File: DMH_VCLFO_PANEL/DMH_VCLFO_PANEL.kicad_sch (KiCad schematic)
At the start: 44 parts, among them J0 Panel_GND_Solder_Wire_Pad

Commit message: Improved ergonomics
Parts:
- removed H17, H27, H6: Square, SynthStuff:Jack_6.35mm_Cutout_Output_v6, symbol SynthStuff:MountingHole_Jack6.35mm_Output_v2
- removed H19, H29, H7: Triangle, SynthStuff:Jack_6.35mm_Cutout_Output_v6, symbol SynthStuff:MountingHole_Jack6.35mm_Output_v2
- added H17, H27, H7: Rmp/Rnd, SynthStuff:Toggle_Switch_TE_Cutout, symbol SynthStuff:MountingHole_ToggleSwitch
- added H19, H29, H6: Sin/Tri, SynthStuff:Toggle_Switch_TE_Cutout, symbol SynthStuff:MountingHole_ToggleSwitch
- H10, H23, H33: value Sine -> Ramp / Random
- H11, H24, H34: value Random -> Triangle / Sine
- H22, H32, H9: value Ramp -> Saw
- H39, H40, H8: value Saw -> Square
- H44, H45, H46: value Unipolar -> Pol
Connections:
- net GND: now also H17.1, H19.1, H27.1, H29.1, H6.1, H7.1

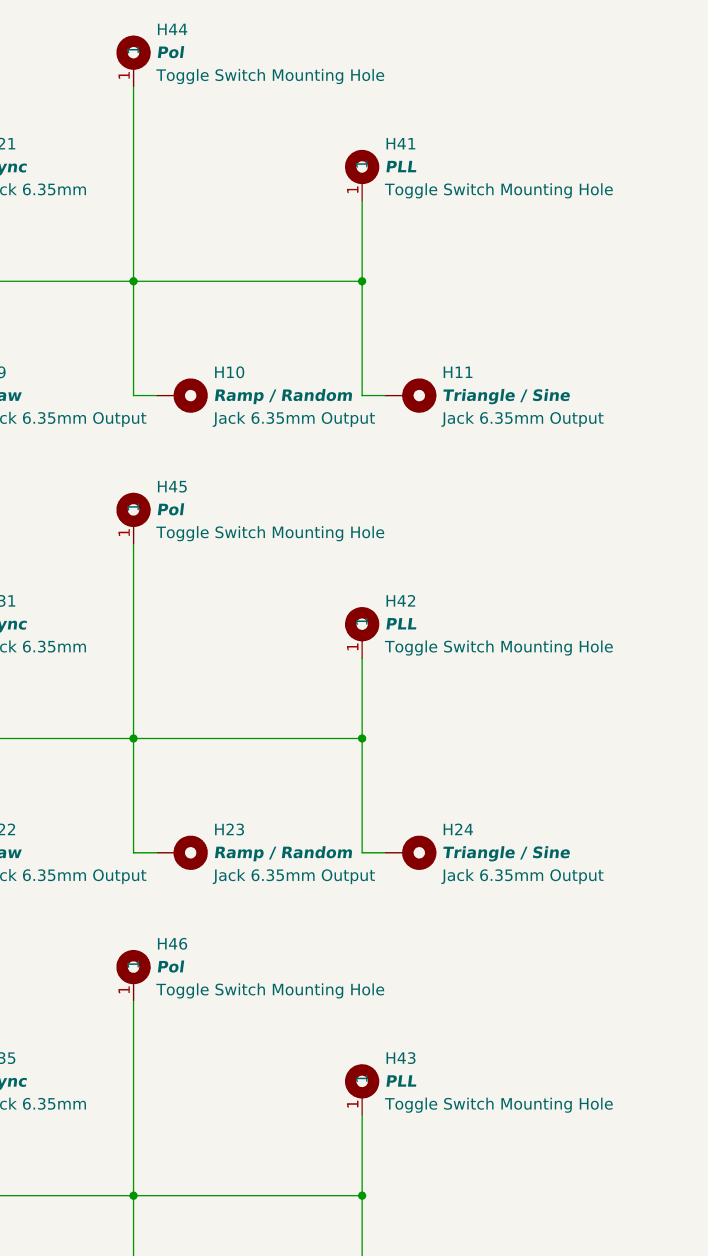
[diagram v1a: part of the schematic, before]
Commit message: Replaced PLL with Range
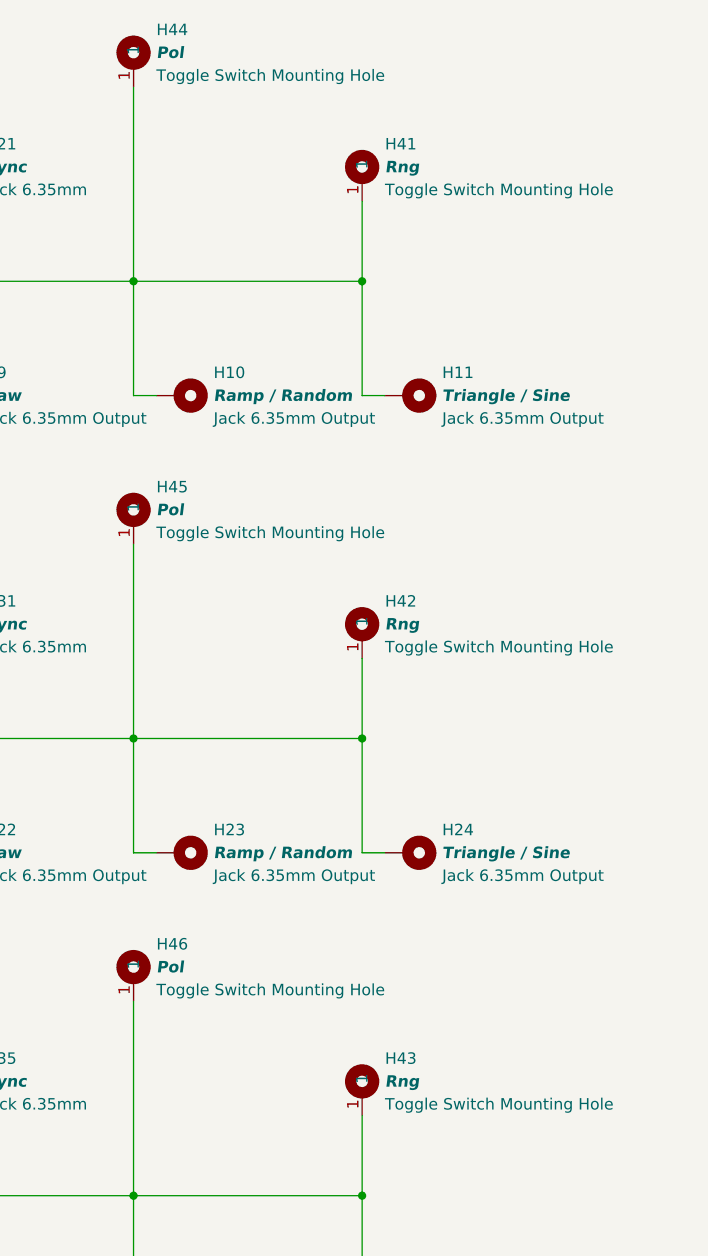
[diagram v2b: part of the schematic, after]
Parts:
- H41, H42, H43: value PLL -> Rng
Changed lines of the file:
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@@
 			)
 		)
-		(property "Value" "PLL"
+		(property "Value" "Rng"
 			(at 161.29 50.8 0)
 			(effects
@@
 			)
 		)
-		(property "Value" "PLL"
+		(property "Value" "Rng"
 			(at 161.29 101.6 0)
 			(effects
@@
 			)
 		)
-		(property "Value" "PLL"
+		(property "Value" "Rng"
 			(at 161.29 152.4 0)
 			(effects

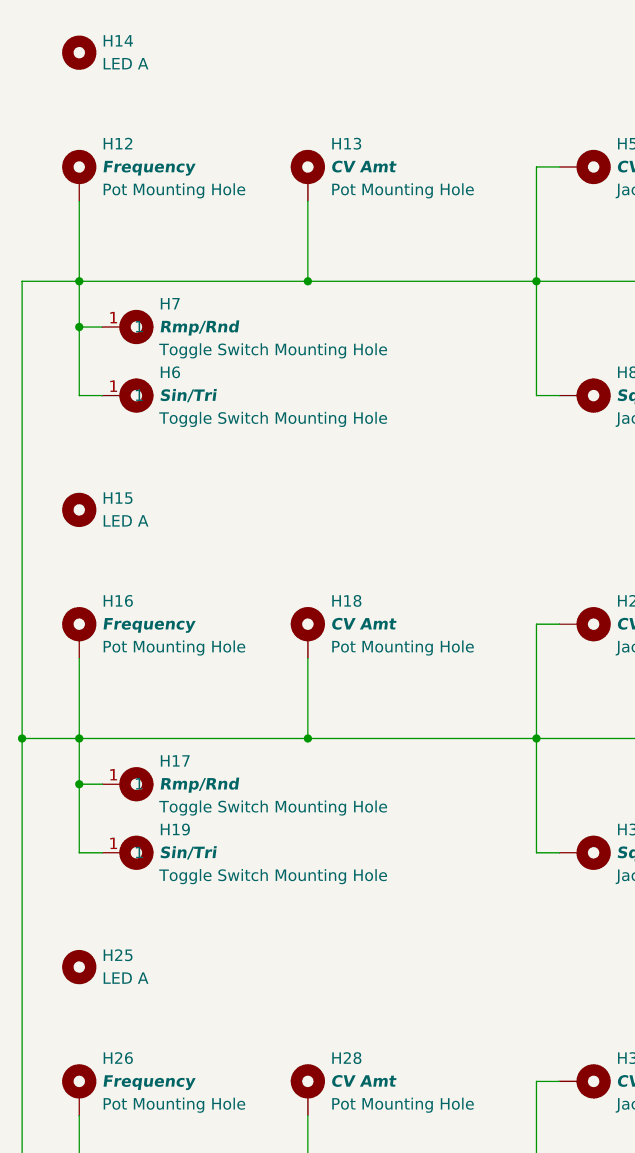
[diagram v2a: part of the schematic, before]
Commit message: Added yellow LED to Panel
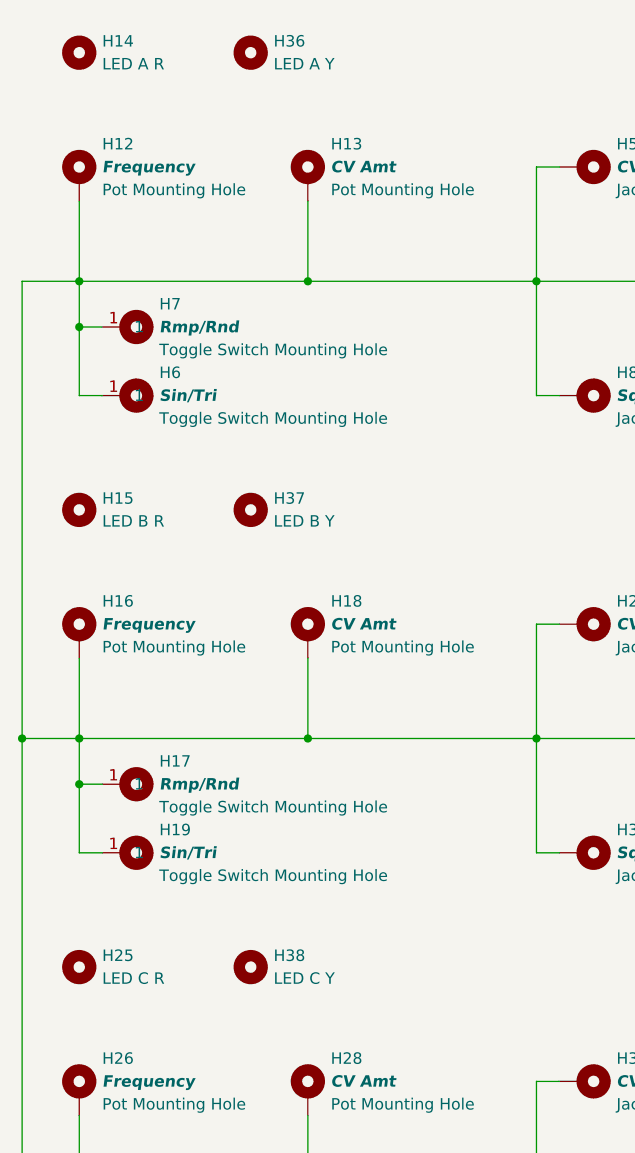
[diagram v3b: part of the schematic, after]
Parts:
- added H36: LED A Y, SynthStuff:MountingHole_LED_3mm_Y, symbol Mechanical:MountingHole
- added H37: LED B Y, SynthStuff:MountingHole_LED_3mm_Y, symbol Mechanical:MountingHole
- added H38: LED C Y, SynthStuff:MountingHole_LED_3mm_Y, symbol Mechanical:MountingHole
- H14: value LED A -> LED A R; footprint SynthStuff:MountingHole_LED_3mm -> SynthStuff:MountingHole_LED_3mm_R
- H15: value LED A -> LED B R; footprint SynthStuff:MountingHole_LED_3mm -> SynthStuff:MountingHole_LED_3mm_R
- H25: value LED A -> LED C R; footprint SynthStuff:MountingHole_LED_3mm -> SynthStuff:MountingHole_LED_3mm_R
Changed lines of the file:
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@@
 			)
 		)
-		(property "Value" "LED A"
+		(property "Value" "LED C R"
 			(at 34.29 140.9699 0)
 			(effects
@@
 			)
 		)
-		(property "Footprint" "SynthStuff:MountingHole_LED_3mm"
+		(property "Footprint" "SynthStuff:MountingHole_LED_3mm_R"
 			(at 31.75 139.7 0)
 			(effects
@@
 	(symbol
 		(lib_id "Mechanical:MountingHole")
+		(at 50.8 139.7 0)
+		(unit 1)
+		(exclude_from_sim no)
+		(in_bom no)
+		(on_board yes)
+		(dnp no)
+		(fields_autoplaced yes)
+		(property "Reference" "H38"
+			(at 53.34 138.4299 0)
+			(effects
+				(font
+					(size 1.27 1.27)
+				)
+				(justify left)
+			)
+		)
+		(property "Value" "LED C Y"
+			(at 53.34 140.9699 0)
+			(effects
+				(font
+					(size 1.27 1.27)
+				)
+				(justify left)
+			)
+		)
+		(property "Footprint" "SynthStuff:MountingHole_LED_3mm_Y"
+			(at 50.8 139.7 0)
+			(effects
+				(font
+					(size 1.27 1.27)
+				)
+				(hide yes)
+			)
+		)
+		(property "Datasheet" "~"
+			(at 50.8 139.7 0)
+			(effects
+				(font
+					(size 1.27 1.27)
+				)
+				(hide yes)
+			)
+		)
+		(property "Description" "Mounting Hole without connection"
+			(at 50.8 139.7 0)
+			(effects
+				(font
+					(size 1.27 1.27)
+				)
+				(hide yes)
+			)
+		)
+		(property "Function" ""
+			(at 50.8 139.7 0)
+			(effects
+				(font
+					(size 1.27 1.27)
+				)
+			)
+		)
+		(instances
+			(project "DMH_VCLFO_PANEL"
+				(path "/a552705f-a9fe-462e-9913-5cfcc08b233c"
+					(reference "H38")
+					(unit 1)
+				)
+			)
+		)
+	)
+	(symbol
+		(lib_id "Mechanical:MountingHole")
 		(at 31.75 38.1 0)
 		(unit 1)
@@
 			)
 		)
-		(property "Value" "LED A"
+		(property "Value" "LED A R"
 			(at 34.29 39.3699 0)
 			(effects
@@
 			)
 		)
-		(property "Footprint" "SynthStuff:MountingHole_LED_3mm"
+		(property "Footprint" "SynthStuff:MountingHole_LED_3mm_R"
 			(at 31.75 38.1 0)
 			(effects
@@
 			)
 		)
-		(property "Value" "LED A"
+		(property "Value" "LED B R"
 			(at 34.29 90.1699 0)
 			(effects
@@
 			)
 		)
-		(property "Footprint" "SynthStuff:MountingHole_LED_3mm"
+		(property "Footprint" "SynthStuff:MountingHole_LED_3mm_R"
 			(at 31.75 88.9 0)
 			(effects
@@
 	)
 	(symbol
+		(lib_id "Mechanical:MountingHole")
+		(at 50.8 38.1 0)
+		(unit 1)
+		(exclude_from_sim no)
+		(in_bom no)
+		(on_board yes)
+		(dnp no)
+		(fields_autoplaced yes)
+		(property "Reference" "H36"
+			(at 53.34 36.8299 0)
+			(effects
+				(font
+					(size 1.27 1.27)
+				)
+				(justify left)
+			)
+		)
+		(property "Value" "LED A Y"
+			(at 53.34 39.3699 0)
+			(effects
+				(font
+					(size 1.27 1.27)
+				)
+				(justify left)
+			)
+		)
+		(property "Footprint" "SynthStuff:MountingHole_LED_3mm_Y"
+			(at 50.8 38.1 0)
+			(effects
+				(font
+					(size 1.27 1.27)
+				)
+				(hide yes)
+			)
+		)
+		(property "Datasheet" "~"
+			(at 50.8 38.1 0)
+			(effects
+				(font
+					(size 1.27 1.27)
+				)
+				(hide yes)
+			)
+		)
+		(property "Description" "Mounting Hole without connection"
+			(at 50.8 38.1 0)
+			(effects
+				(font
+					(size 1.27 1.27)
+				)
+				(hide yes)
+			)
+		)
+		(property "Function" ""
+			(at 50.8 38.1 0)
+			(effects
+				(font
+					(size 1.27 1.27)
+				)
+			)
+		)
+		(instances
+			(project "DMH_VCLFO_PANEL"
+				(path "/a552705f-a9fe-462e-9913-5cfcc08b233c"
+					(reference "H36")
+					(unit 1)
+				)
+			)
+		)
+	)
+	(symbol
 		(lib_id "SynthStuff:MountingHole_ToggleSwitch")
 		(at 133.35 38.1 0)
@@
 					(unit 1)
 				)
+			)
+		)
+	)
+	(symbol
+		(lib_id "Mechanical:MountingHole")
+		(at 50.8 88.9 0)
+		(unit 1)
+		(exclude_from_sim no)
+		(in_bom no)
+		(on_board yes)
+		(dnp no)
+		(fields_autoplaced yes)
+		(property "Reference" "H37"
+			(at 53.34 87.6299 0)
+			(effects
+				(font
+					(size 1.27 1.27)
+				)
+				(justify left)
+			)
+		)
+		(property "Value" "LED B Y"
+			(at 53.34 90.1699 0)
+			(effects
+				(font
+					(size 1.27 1.27)
+				)
+				(justify left)
+			)
+		)
+		(property "Footprint" "SynthStuff:MountingHole_LED_3mm_Y"
+			(at 50.8 88.9 0)
+			(effects
+				(font
+					(size 1.27 1.27)
+				)
+				(hide yes)
+			)
+		)
+		(property "Datasheet" "~"
+			(at 50.8 88.9 0)
+			(effects
+				(font
+					(size 1.27 1.27)
+				)
+				(hide yes)
+			)
+		)
+		(property "Description" "Mounting Hole without connection"
+			(at 50.8 88.9 0)
+			(effects
+				(font
+					(size 1.27 1.27)
+				)
+				(hide yes)
+			)
+		)
+		(property "Function" ""
+			(at 50.8 88.9 0)
+			(effects
+				(font
+					(size 1.27 1.27)
+				)
+			)
+		)
+		(instances
+			(project "DMH_VCLFO_PANEL"
+				(path "/a552705f-a9fe-462e-9913-5cfcc08b233c"
+					(reference "H37")
+					(unit 1)
+				)
